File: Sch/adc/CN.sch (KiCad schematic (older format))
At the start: 25 parts, among them J1 JP2, J2 JP2, P1 CONN_02X40, U1 LTC2292

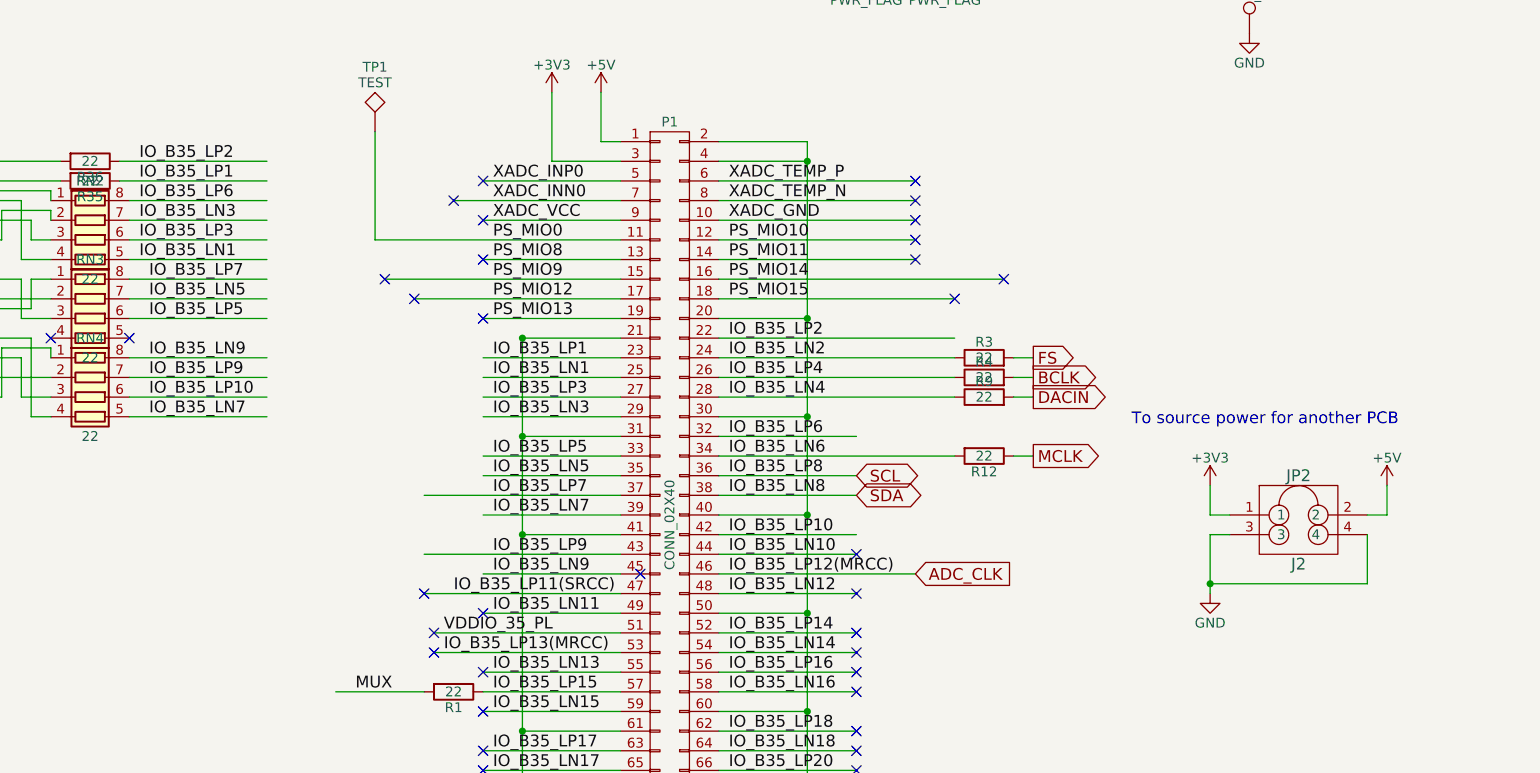
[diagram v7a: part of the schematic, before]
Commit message: ADC Layout done except GND
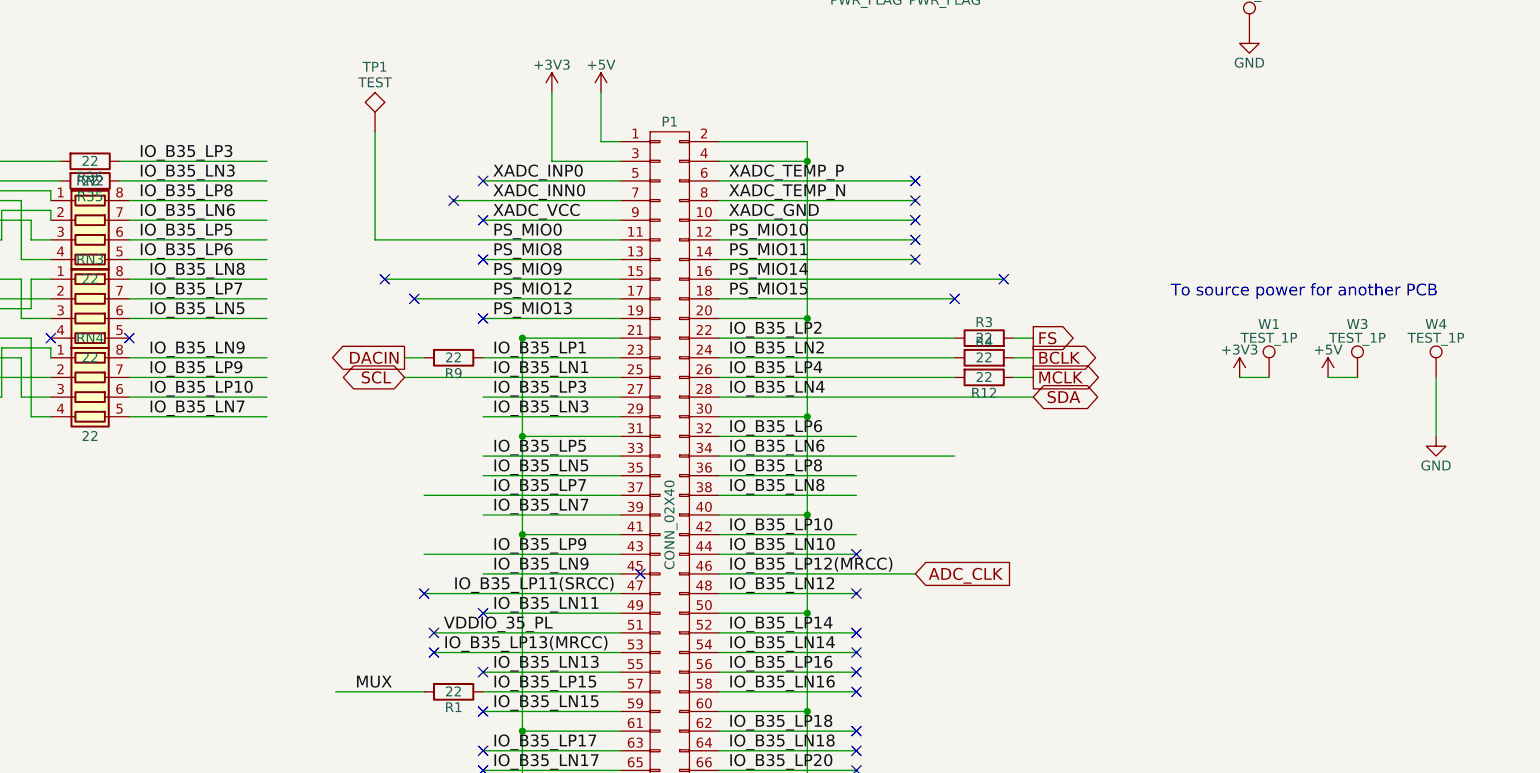
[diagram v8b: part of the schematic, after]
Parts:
- removed J2: JP2, adc_lib:M20-9980245, symbol JP2
- added W1, W3, W4: TEST_1P, adc_lib:68000-401HLF, symbol TEST_1P
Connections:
- wire segments 169 -> 164
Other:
- moved on the sheet: R12, R3, R4, R9
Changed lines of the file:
@@
 Text Label 4250 2850 0    60   ~ 0
 IO_B35_LN9
+Text Label 4250 2550 0    60   ~ 0
+IO_B35_LP7
+Text Label 4250 2650 0    60   ~ 0
+IO_B35_LN5
+Text Label 4200 2250 0    60   ~ 0
+IO_B35_LP5
+Text Label 4200 2350 0    60   ~ 0
+IO_B35_LP6
 Text Label 4250 2450 0    60   ~ 0
-IO_B35_LP7
-Text Label 4250 2550 0    60   ~ 0
-IO_B35_LN5
-Text Label 4250 2650 0    60   ~ 0
-IO_B35_LP5
+IO_B35_LN8
 Text Label 4200 2050 0    60   ~ 0
-IO_B35_LP6
+IO_B35_LP8
+Text Label 4200 1850 0    60   ~ 0
+IO_B35_LP3
 Text Label 4200 1950 0    60   ~ 0
-IO_B35_LP1
-Text Label 4200 2350 0    60   ~ 0
-IO_B35_LN1
-Text Label 4200 2250 0    60   ~ 0
-IO_B35_LP3
+IO_B35_LN3
 Text Label 4200 2150 0    60   ~ 0
-IO_B35_LN3
-Text Label 4200 1850 0    60   ~ 0
-IO_B35_LP2
+IO_B35_LN6
 Text Label 1550 2800 0    60   ~ 0
 SHDNA
@@
 Text Notes 750  3300 0    60   ~ 0
 High=nap mode
+Text GLabel 8750 2750 2    60   Output ~ 0
+FS
 Text GLabel 8750 2850 2    60   Output ~ 0
-FS
+BCLK
+Text GLabel 5550 2850 0    60   Output ~ 0
+DACIN
 Text GLabel 8750 2950 2    60   Output ~ 0
-BCLK
-Text GLabel 8750 3050 2    60   Output ~ 0
-DACIN
-Text GLabel 8750 3350 2    60   Output ~ 0
 MCLK
-Text GLabel 7850 3450 2    60   BiDi ~ 0
+Text GLabel 5550 2950 0    60   BiDi ~ 0
 SCL
-Text GLabel 7850 3550 2    60   BiDi ~ 0
+Text GLabel 8750 3050 2    60   BiDi ~ 0
 SDA
 $Comp
 L R R12
 U 1 1 58A9A823
-P 8500 3350
-F 0 "R12" V 8580 3350 50  0000 C CNN
-F 1 "22" V 8500 3350 50  0000 C CNN
-F 2 "adc_lib:R0603" V 8430 3350 50  0001 C CNN
-F 3 "" H 8500 3350 50  0000 C CNN
-	1    8500 3350
+P 8500 2950
+F 0 "R12" V 8580 2950 50  0000 C CNN
+F 1 "22" V 8500 2950 50  0000 C CNN
+F 2 "adc_lib:R0603" V 8430 2950 50  0001 C CNN
+F 3 "" H 8500 2950 50  0000 C CNN
+	1    8500 2950
 	0    1    1    0
 $EndComp
@@
 L R R4
 U 1 1 59574E56
-P 8500 2950
-F 0 "R4" V 8580 2950 50  0000 C CNN
-F 1 "22" V 8500 2950 50  0000 C CNN
-F 2 "adc_lib:R0603" V 8430 2950 50  0001 C CNN
-F 3 "" H 8500 2950 50  0000 C CNN
-	1    8500 2950
-	0    -1   -1   0
-$EndComp
-$Comp
-L R R3
-U 1 1 59574F08
 P 8500 2850
-F 0 "R3" V 8580 2850 50  0000 C CNN
+F 0 "R4" V 8580 2850 50  0000 C CNN
 F 1 "22" V 8500 2850 50  0000 C CNN
 F 2 "adc_lib:R0603" V 8430 2850 50  0001 C CNN
@@
 $EndComp
 $Comp
+L R R3
+U 1 1 59574F08
+P 8500 2750
+F 0 "R3" V 8580 2750 50  0000 C CNN
+F 1 "22" V 8500 2750 50  0000 C CNN
+F 2 "adc_lib:R0603" V 8430 2750 50  0001 C CNN
+F 3 "" H 8500 2750 50  0000 C CNN
+	1    8500 2750
+	0    -1   -1   0
+$EndComp
+$Comp
 L R R9
 U 1 1 59574F5D
-P 8500 3050
-F 0 "R9" V 8580 3050 50  0000 C CNN
-F 1 "22" V 8500 3050 50  0000 C CNN
-F 2 "adc_lib:R0603" V 8430 3050 50  0001 C CNN
-F 3 "" H 8500 3050 50  0000 C CNN
-	1    8500 3050
-	0    -1   -1   0
+P 5800 2850
+F 0 "R9" V 5880 2850 50  0000 C CNN
+F 1 "22" V 5800 2850 50  0000 C CNN
+F 2 "adc_lib:R0603" V 5730 2850 50  0001 C CNN
+F 3 "" H 5800 2850 50  0000 C CNN
+	1    5800 2850
+	0    1    1    0
 $EndComp
 $Comp
 L +3V3 #PWR015
 U 1 1 59761EBD
-P 9650 3500
-F 0 "#PWR015" H 9650 3350 50  0001 C CNN
-F 1 "+3V3" H 9650 3640 50  0000 C CNN
-F 2 "" H 9650 3500 50  0000 C CNN
-F 3 "" H 9650 3500 50  0000 C CNN
-	1    9650 3500
+P 9800 2950
+F 0 "#PWR015" H 9800 2800 50  0001 C CNN
+F 1 "+3V3" H 9800 3090 50  0000 C CNN
+F 2 "" H 9800 2950 50  0000 C CNN
+F 3 "" H 9800 2950 50  0000 C CNN
+	1    9800 2950
 	1    0    0    -1
 $EndComp
@@
 L +5V #PWR016
 U 1 1 59761EC3
-P 10550 3500
-F 0 "#PWR016" H 10550 3350 50  0001 C CNN
-F 1 "+5V" H 10550 3640 50  0000 C CNN
-F 2 "" H 10550 3500 50  0000 C CNN
-F 3 "" H 10550 3500 50  0000 C CNN
-	1    10550 3500
+P 10250 2950
+F 0 "#PWR016" H 10250 2800 50  0001 C CNN
+F 1 "+5V" H 10250 3090 50  0000 C CNN
+F 2 "" H 10250 2950 50  0000 C CNN
+F 3 "" H 10250 2950 50  0000 C CNN
+	1    10250 2950
 	1    0    0    -1
 $EndComp
@@
 L GND #PWR017
 U 1 1 59762403
-P 9650 4050
-F 0 "#PWR017" H 9650 3800 50  0001 C CNN
-F 1 "GND" H 9650 3900 50  0000 C CNN
-F 2 "" H 9650 4050 50  0000 C CNN
-F 3 "" H 9650 4050 50  0000 C CNN
-	1    9650 4050
-	1    0    0    -1
-$EndComp
-$Comp
-L JP2 J2
-U 1 1 59776382
-P 10100 3650
-F 0 "J2" H 10100 3400 60  0000 C CNN
-F 1 "JP2" H 10100 3850 60  0000 C CNN
-F 2 "adc_lib:M20-9980245" H 10050 3750 60  0001 C CNN
-F 3 "" H 10050 3750 60  0001 C CNN
-	1    10100 3650
+P 10800 3250
+F 0 "#PWR017" H 10800 3000 50  0001 C CNN
+F 1 "GND" H 10800 3100 50  0000 C CNN
+F 2 "" H 10800 3250 50  0000 C CNN
+F 3 "" H 10800 3250 50  0000 C CNN
+	1    10800 3250
 	1    0    0    -1
 $EndComp
 Text Notes 750  2200 0    60   ~ 0
 SHDN, MUX=3.3V (3.0 V is better)
-Text Notes 9250 3200 0    60   ~ 0
+Text Notes 9450 2550 0    60   ~ 0
 To source power for another PCB
 $Comp
@@
 	6650 3450 5950 3450
 Wire Wire Line
-	6650 2950 5950 2950
+	5550 2950 6650 2950
 Wire Wire Line
 	6300 1500 6300 1850
@@
 	7150 2950 8350 2950
 Wire Wire Line
-	7150 3050 8350 3050
+	7150 3050 8750 3050
 Wire Wire Line
 	7150 3250 7850 3250
@@
 	4850 2450 4150 2450
 Wire Wire Line
+	4850 2650 4150 2650
+Wire Wire Line
 	4850 2550 4150 2550
-Wire Wire Line
-	4850 2650 4150 2650
 Wire Wire Line
 	4100 1950 4850 1950
@@
 Connection ~ 3150 6050
 Wire Wire Line
+	8750 2750 8650 2750
+Wire Wire Line
 	8750 2850 8650 2850
 Wire Wire Line
+	5550 2850 5650 2850
+Wire Wire Line
 	8750 2950 8650 2950
 Wire Wire Line
-	8750 3050 8650 3050
-Wire Wire Line
-	8750 3350 8650 3350
-Wire Wire Line
-	9750 3750 9650 3750
-Wire Wire Line
-	9650 3750 9650 4050
-Wire Wire Line
-	10450 3750 10450 4000
-Wire Wire Line
-	10450 4000 9650 4000
-Connection ~ 9650 4000
-Wire Wire Line
-	9650 3500 9650 3650
-Wire Wire Line
-	9650 3650 9750 3650
-Wire Wire Line
-	10450 3650 10550 3650
-Wire Wire Line
-	10550 3650 10550 3500
+	10800 2950 10800 3250
 Wire Wire Line
 	5400 1700 5400 2250
@@
 NoConn ~ 7850 4350
 NoConn ~ 6750 3950
+$Comp
+L TEST_1P W1
+U 1 1 5981C0B7
+P 9950 2950
+F 0 "W1" H 9950 3220 50  0000 C CNN
+F 1 "TEST_1P" H 9950 3150 50  0000 C CNN
+F 2 "adc_lib:68000-401HLF" H 10150 2950 50  0001 C CNN
+F 3 "" H 10150 2950 50  0000 C CNN
+	1    9950 2950
+	1    0    0    -1
+$EndComp
+$Comp
+L TEST_1P W3
+U 1 1 5981C106
+P 10400 2950
+F 0 "W3" H 10400 3220 50  0000 C CNN
+F 1 "TEST_1P" H 10400 3150 50  0000 C CNN
+F 2 "adc_lib:68000-401HLF" H 10600 2950 50  0001 C CNN
+F 3 "" H 10600 2950 50  0000 C CNN
+	1    10400 2950
+	1    0    0    -1
+$EndComp
+$Comp
+L TEST_1P W4
+U 1 1 5981C15B
+P 10800 2950
+F 0 "W4" H 10800 3220 50  0000 C CNN
+F 1 "TEST_1P" H 10800 3150 50  0000 C CNN
+F 2 "adc_lib:68000-401HLF" H 11000 2950 50  0001 C CNN
+F 3 "" H 11000 2950 50  0000 C CNN
+	1    10800 2950
+	1    0    0    -1
+$EndComp
+Wire Wire Line
+	9800 2950 9950 2950
+Wire Wire Line
+	10250 2950 10400 2950
 $EndSCHEMATC
